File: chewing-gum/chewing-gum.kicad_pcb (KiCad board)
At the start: 2 copper layers, 25.1 x 52.8 mm, 22 parts, among them IC9 INA212AIDCKR, J15 Conn_02x01, J23 Conn_02x01, J28 Conn_01x03, J36 Conn_01x01_Socket, J42 Conn_Coaxial, J62 Conn_01x01_Socket, J78 Conn_01x03, U21 TLV75801PDBV

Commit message: First version of the chewing gum Vdc
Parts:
- removed J62: Conn_01x01_Socket, TestPoint:TestPoint_Keystone_5019_Minature
- removed R93: 48.7k, Resistor_SMD:R_0603_1608Metric
- removed TGND4: TestPoint, TestPoint:TestPoint_THTPad_4.0x4.0mm_Drill2.0mm
- removed TPVBLD3: TestPoint, TestPoint:TestPoint_Plated_Hole_D2.0mm
- added G***: LOGO, heep_footprints:ESL_3x3, B.Cu at (144.8, 59.1)
- added G***: LOGO, heep_footprints:EPFL_2x7, B.Cu at (138.3, 59.1)
- added J10: Conn_01x04, Connector_PinHeader_1.27mm:PinHeader_1x04_P1.27mm_Vertical, F.Cu at (145.9, 102.0)
- added J11: Conn_02x01, Connector_PinHeader_2.54mm:PinHeader_1x02_P2.54mm_Vertical, F.Cu at (136.1, 98.0)
- added J7: Conn_01x06, Connector_PinHeader_1.27mm:PinHeader_1x06_P1.27mm_Vertical, F.Cu at (135.1, 81.0)
- added J8: Conn_01x06, Connector_PinHeader_1.27mm:PinHeader_1x06_P1.27mm_Vertical, F.Cu at (145.8, 81.1)
- added J9: Conn_01x04, Connector_PinHeader_1.27mm:PinHeader_1x04_P1.27mm_Vertical, F.Cu at (135.3, 101.8)
- added R4: 48.7k, Resistor_SMD:R_0603_1608Metric, F.Cu at (138.1, 69.2)
- moved J6 40.8 mm to (137.1, 116.7)
- moved RV1 35.9 mm to (139.9, 85.9), turned to -90 degrees
- moved J3 28.2 mm to (135.3, 78.0), turned to 180 degrees
- moved C2 26.6 mm to (141.2, 90.5)
- moved J4 25.4 mm to (138.6, 90.6), turned to -90 degrees
- moved J2 23.0 mm to (142.8, 96.6)
- moved R1 22.1 mm to (140.5, 67.0)
- moved R5 21.5 mm to (138.8, 77.5)
- moved IC1 21.1 mm to (143.4, 90.8), turned to -90 degrees
- moved R6 20.7 mm to (136.1, 96.7)
- moved D1 19.1 mm to (140.5, 68.6), turned to 0 degrees
- moved R2 18.7 mm to (140.5, 70.2), turned to 180 degrees
- moved R3 18.5 mm to (138.3, 73.0), turned to -90 degrees
- moved C3 18.0 mm to (138.8, 76.0), turned to 180 degrees
- moved J5 17.1 mm to (138.9, 102.6)
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- renumbered C57 to C1, C41 to C2, C58 to C3, IC9 to IC1, J28 to J1, J42 to J2, J78 to J3, J15 to J4, J23 to J5, J36 to J6, R49 to R1, R34 to R2, R41 to R3, R42 to R5, R20 to R6, RV5 to RV1, U21 to U1
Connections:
- net /V_B3_load_n renamed /V_out_test_n
- net /V_B3_o renamed /V_diff_ampl_out
- net /vblade3_ldo renamed /V_ldo_out
- net Net-(J78-Pin_2) renamed /V_ldo_feedback
- C2 pad 1: +3.3VA -> /3V3
- IC1 pad 3: +3.3VA -> /3V3
- IC1 pad 4: /V_B3_INA -> /V_out_test_p
- J1 pad 1: /3V3_LDO -> /3V3
- J1 pad 3: /EN_VBLADE3 -> /LDO_EN_EXT
- J3 pad 3: /DAC4 -> /DAC_ctrl
- J4 pad 2: /V_B3_INA -> /V_out_test_p
- J5 pad 2: /V_B3_load -> /V_out
- J6 pad 1: /V_B3_INA -> /V_out
- R6 pad 2: /V_B3_INA -> /V_out_test_p
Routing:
- net GND: track 29.7 -> 0.00 mm, vias 7 -> 67
- net /EN_VBLADE3: track 26.1 -> 0.00 mm, vias 1 -> 0
- net /V_B3_INA: track 25.8 -> 0.00 mm
- net /V_B3_load: track 17.7 -> 0.00 mm, vias 1 -> 0
- net /DAC_ctrl: track 0.00 -> 15.8 mm
- net /V_out_test_p: track 0.00 -> 12.4 mm
- net /LDO_EN_EXT: track 0.00 -> 9.71 mm
- net /V_out: track 0.00 -> 8.92 mm
- net /V_diff_ampl_out: track 8.79 -> 16.0 mm
- net Net-(D1-A): track 15.7 -> 9.81 mm
- net /V_out_test_n: track 14.3 -> 18.0 mm
- net /V_ldo_out: track 17.5 -> 21.1 mm, vias 3 -> 0
- net /DAC4: track 2.98 -> 0.00 mm
- net +3.3VA: track 2.15 -> 0.00 mm, vias 1 -> 0
- net Net-(R5-Pad1): track 5.16 -> 3.42 mm
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- added copper zone on B.Cu, net (none)
- added copper zone on F.Cu, net /3V3
- added copper zone on F.Cu, net /V_ldo_feedback
- added copper zone on B.Cu, net GND
- added copper zone on F.Cu, net GND
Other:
- board size 25.1 x 52.8 mm -> 13.1 x 49.3 mm
- board text added: "(LDO)"
- board text added: "(ampl)"
- board text added: "(shunt)"
- board text added: "(trimmer)"
- board text added: "+-"
- board text added: "Chewing-gum: V - v1.0 - 09/25"
- board text added: "DAC ctrl▶"
- board text added: "DC"
- board text added: "Ext. En"
- board text added: "GND"
- board text added: "LDO fb▶"
- board text added: "LDOout◀"
- board text added: "NC"
- board text added: "R6←LDO"
- board text added: "R6→out"
- board text added: "Vout"
- board text added: "▶"
- board text added: "▶Vdiff"
- board text added: "◀3V3"
- board text added: "◀Ext. EN"
- board text added: "◀Ref.Ampl."
- board text removed: "I2C enable"
- board text removed: "VBLADE2"

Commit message: Finished ADC/DAC board
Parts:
- removed J6: Conn_01x01_Socket, Connector:Banana_Jack_1Pin
- moved J9 0.38 mm to (135.1, 102.1)
- moved J8 0.10 mm to (145.9, 81.0)
- moved J7 0.07 mm to (135.1, 81.0)
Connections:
- J10 pad 3: /V_diff_ampl_out -> unconnected-(J10-Pin_3-Pad3)
- J10 pad 4: unconnected-(J10-Pin_4-Pad4) -> /V_diff_ampl_out
- J8 pad 3: GND -> unconnected-(J8-Pin_3-Pad3)
- J8 pad 4: unconnected-(J8-Pin_4-Pad4) -> GND
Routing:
- net /V_out: track 8.92 -> 0.62 mm
- net /V_diff_ampl_out: track 16.0 -> 16.8 mm
- net GND: vias 67 -> 71
- added copper zone on F.Cu, net /V_out

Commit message: Before re-organizing the main board
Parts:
- moved C1 1.66 mm to (141.8, 75.3), turned to 180 degrees
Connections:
- C1 pad 1: /Vpm -> /5V
- J8 pad 2: unconnected-(J8-Pin_2-Pad2) -> /5V
- J8 pad 3: unconnected-(J8-Pin_3-Pad3) -> /5V
- U1 pad 1: /Vpm -> /5V
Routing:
- net /Vpm: track 2.43 -> 0.00 mm
- net GND: vias 71 -> 68
- added copper zone on F.Cu, net /5V
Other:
- board text added: "◀5V"

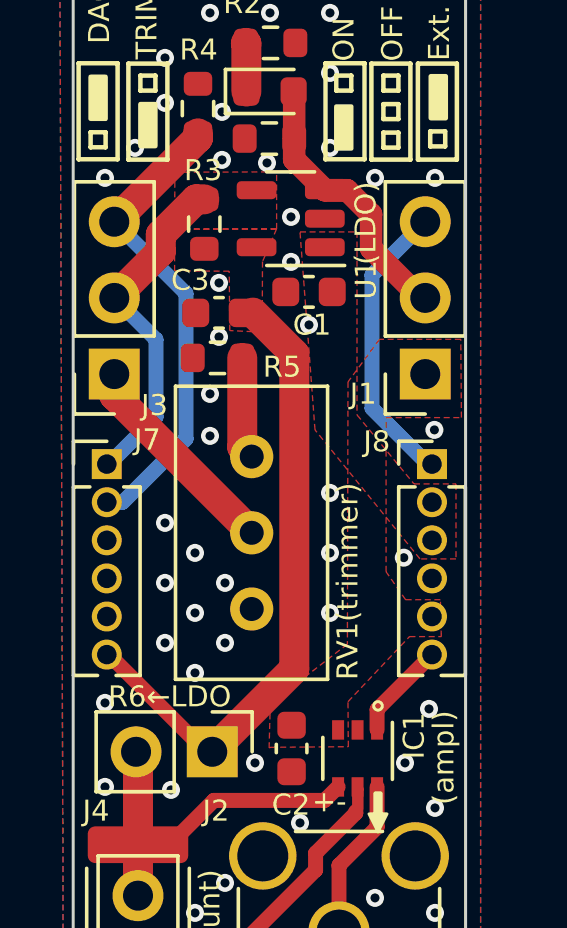
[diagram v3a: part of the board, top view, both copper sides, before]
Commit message: Before re-routing programmer
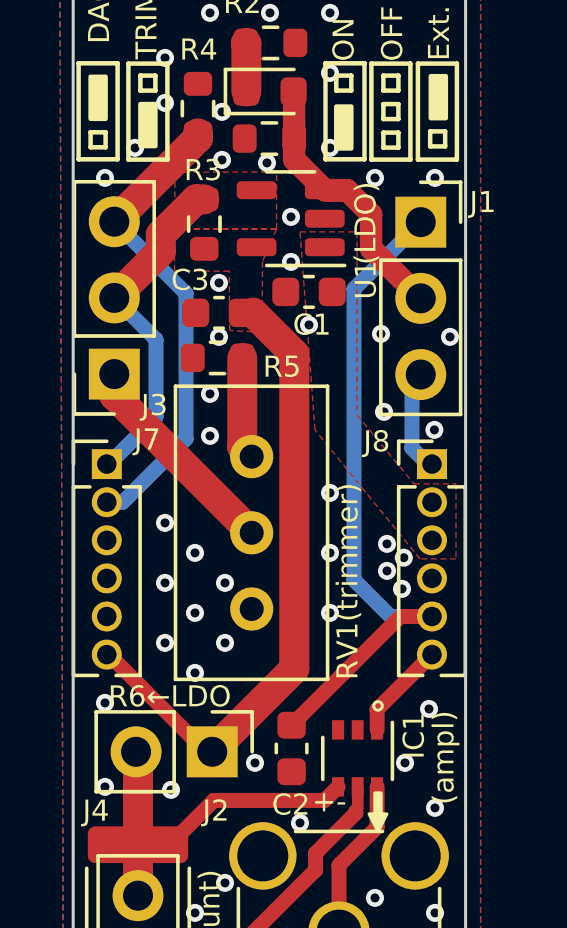
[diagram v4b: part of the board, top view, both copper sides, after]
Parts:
- moved J1 5.07 mm to (145.5, 73.0), turned to 0 degrees
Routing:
- net /3V3: track 0.00 -> 22.1 mm
- net /LDO_EN_EXT: track 9.71 -> 3.45 mm
- net GND: vias 68 -> 74
- removed copper zone on F.Cu, net /3V3
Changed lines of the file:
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@@
 	(footprint "Connector_PinSocket_2.54mm:PinSocket_1x03_P2.54mm_Vertical"
 		(layer "F.Cu")
-		(at 145.675 78.04 180)
+		(at 145.525 72.975)
 		(descr "Through hole straight socket strip, 1x03, 2.54mm pitch, single row (from Kicad 4.0.7), script generated")
 		(tags "Through hole socket strip THT 1x03 2.54mm single row")
 		(property "Reference" "J1"
-			(at 2.07 -0.66 0)
+			(at 2.07 -0.66 360)
 			(layer "F.SilkS")
 			(effects
@@
 		)
 		(property "Value" "Conn_01x03"
-			(at 0 7.85 0)
+			(at 0 7.85 360)
 			(layer "F.Fab")
 			(effects
@@
 		)
 		(property "Footprint" "Connector_PinSocket_2.54mm:PinSocket_1x03_P2.54mm_Vertical"
-			(at 0 0 0)
+			(at 0 0 360)
 			(layer "F.Fab")
 			(hide yes)
@@
 		)
 		(property "Datasheet" ""
-			(at 0 0 0)
+			(at 0 0 360)
 			(layer "F.Fab")
 			(hide yes)
@@
 		)
 		(property "Description" ""
-			(at 0 0 0)
+			(at 0 0 360)
 			(layer "F.Fab")
 			(hide yes)
@@
 		(attr through_hole exclude_from_pos_files)
 		(fp_line
-			(start 1.33 1.27)
-			(end 1.33 6.41)
+			(start -1.33 1.27)
+			(end -1.33 6.41)
 			(stroke
 				(width 0.12)
@@
 		)
 		(fp_line
-			(start 1.33 -1.33)
-			(end 1.33 0)
+			(start -1.33 1.27)
+			(end 1.33 1.27)
 			(stroke
 				(width 0.12)
@@
 		)
 		(fp_line
-			(start 0 -1.33)
-			(end 1.33 -1.33)
+			(start -1.33 6.41)
+			(end 1.33 6.41)
 			(stroke
 				(width 0.12)
@@
 		)
 		(fp_line
-			(start -1.33 6.41)
-			(end 1.33 6.41)
+			(start 0 -1.33)
+			(end 1.33 -1.33)
 			(stroke
 				(width 0.12)
@@
 		)
 		(fp_line
-			(start -1.33 1.27)
-			(end 1.33 1.27)
+			(start 1.33 -1.33)
+			(end 1.33 0)
 			(stroke
 				(width 0.12)
@@
 		)
 		(fp_line
-			(start -1.33 1.27)
-			(end -1.33 6.41)
+			(start 1.33 1.27)
+			(end 1.33 6.41)
 			(stroke
 				(width 0.12)
@@
 		)
 		(fp_line
-			(start 1.75 6.85)
-			(end -1.8 6.85)
+			(start -1.8 -1.8)
+			(end 1.75 -1.8)
 			(stroke
 				(width 0.05)
@@
 		)
 		(fp_line
-			(start 1.75 -1.8)
-			(end 1.75 6.85)
+			(start -1.8 6.85)
+			(end -1.8 -1.8)
 			(stroke
 				(width 0.05)
@@
 		)
 		(fp_line
-			(start -1.8 6.85)
-			(end -1.8 -1.8)
+			(start 1.75 -1.8)
+			(end 1.75 6.85)
 			(stroke
 				(width 0.05)
@@
 		)
 		(fp_line
-			(start -1.8 -1.8)
-			(end 1.75 -1.8)
+			(start 1.75 6.85)
+			(end -1.8 6.85)
 			(stroke
 				(width 0.05)
@@
 		)
 		(fp_line
-			(start 1.27 6.35)
-			(end -1.27 6.35)
+			(start -1.27 -1.27)
+			(end 0.635 -1.27)
 			(stroke
 				(width 0.1)
@@
 		)
 		(fp_line
-			(start 1.27 -0.635)
-			(end 1.27 6.35)
+			(start -1.27 6.35)
+			(end -1.27 -1.27)
 			(stroke
 				(width 0.1)
@@
 		)
 		(fp_line
-			(start -1.27 6.35)
-			(end -1.27 -1.27)
+			(start 1.27 -0.635)
+			(end 1.27 6.35)
 			(stroke
 				(width 0.1)
@@
 		)
 		(fp_line
-			(start -1.27 -1.27)
-			(end 0.635 -1.27)
+			(start 1.27 6.35)
+			(end -1.27 6.35)
 			(stroke
 				(width 0.1)
@@
 		)
 		(pad "1" thru_hole rect
-			(at 0 0 180)
+			(at 0 0)
 			(size 1.7 1.7)
 			(drill 1)
@@
 		)
 		(pad "2" thru_hole oval
-			(at 0 2.54 180)
+			(at 0 2.54)
 			(size 1.7 1.7)
 			(drill 1)
@@
 		)
 		(pad "3" thru_hole oval
-			(at 0 5.08 180)
+			(at 0 5.08)
 			(size 1.7 1.7)
 			(drill 1)
@@
 		)
 		(property "Value" "10u"
-			(at 0 1.43 360)
+			(at 0 1.43 0)
 			(layer "F.Fab")
 			(effects
@@
 		)
 		(property "Footprint" "Capacitor_SMD:C_0603_1608Metric"
-			(at 0 0 360)
+			(at 0 0 0)
 			(layer "F.Fab")
 			(hide yes)
@@
 		)
 		(property "Datasheet" ""
-			(at 0 0 360)
+			(at 0 0 0)
 			(layer "F.Fab")
 			(hide yes)
@@
 		)
 		(property "Description" ""
-			(at 0 0 360)
+			(at 0 0 0)
 			(layer "F.Fab")
 			(hide yes)
@@
 		)
 		(fp_text user "${REFERENCE}"
-			(at 0 0 360)
+			(at 0 0 0)
 			(layer "F.Fab")
 			(effects
@@
 	)
 	(via
+		(at 144.4 84.6)
+		(size 0.6)
+		(drill 0.3)
+		(layers "F.Cu" "B.Cu")
+		(free yes)
+		(net 1)
+	)
+	(via
 		(at 144.5 106)
 		(size 0.6)
@@
 	)
 	(via
+		(at 144.2 76.7)
+		(size 0.6)
+		(drill 0.3)
+		(layers "F.Cu" "B.Cu")
+		(free yes)
+		(net 1)
+	)
+	(via
 		(at 139 95)
 		(size 0.6)
@@
 	)
 	(via
+		(at 144.3 79.3)
+		(size 0.6)
+		(drill 0.3)
+		(layers "F.Cu" "B.Cu")
+		(free yes)
+		(net 1)
+	)
+	(via
 		(at 135 71.5)
 		(size 0.6)
@@
 	)
 	(via
+		(at 146.5 76.8)
+		(size 0.6)
+		(drill 0.3)
+		(layers "F.Cu" "B.Cu")
+		(free yes)
+		(net 1)
+	)
+	(via
 		(at 138.8 75)
 		(size 0.6)
@@
 	)
 	(via
+		(at 144.4 83.7)
+		(size 0.6)
+		(drill 0.3)
+		(layers "F.Cu" "B.Cu")
+		(free yes)
+		(net 1)
+	)
+	(via
 		(at 138.8 76.8)
 		(size 0.6)
@@
 		(net 1)
 	)
+	(via
+		(at 144.9 85.2)
+		(size 0.6)
+		(drill 0.3)
+		(layers "F.Cu" "B.Cu")
+		(free yes)
+		(net 1)
+	)
 	(segment
 		(start 139.7125 67.0175)
@@
 	)
 	(segment
-		(start 143.9 74.735)
-		(end 145.675 72.96)
+		(start 144.845 86.12)
+		(end 145.9 86.12)
+		(width 0.5)
+		(layer "F.Cu")
+		(net 6)
+	)
+	(segment
+		(start 141.22 89.745)
+		(end 144.845 86.12)
+		(width 0.5)
+		(layer "F.Cu")
+		(net 6)
+	)
+	(segment
+		(start 144.52 86.12)
+		(end 143.3 84.9)
+		(width 0.5)
+		(layer "B.Cu")
+		(net 6)
+	)
+	(segment
+		(start 143.3 84.9)
+		(end 143.3 75.2)
+		(width 0.5)
+		(layer "B.Cu")
+		(net 6)
+	)
+	(segment
+		(start 145.9 86.12)
+		(end 144.52 86.12)
+		(width 0.5)
+		(layer "B.Cu")
+		(net 6)
+	)
+	(segment
+		(start 143.3 75.2)
+		(end 145.525 72.975)
+		(width 0.5)
+		(layer "B.Cu")
+		(net 6)
+	)
+	(segment
+		(start 145.23 78.35)
+		(end 145.525 78.055)
 		(width 0.5)
 		(layer "B.Cu")
@@
 	(segment
 		(start 145.85 81.13)
-		(end 143.9 79.18)
+		(end 145.23 80.51)
 		(width 0.5)
 		(layer "B.Cu")
@@
 	)
 	(segment
-		(start 143.9 79.18)
-		(end 143.9 74.735)
+		(start 145.23 80.51)
+		(end 145.23 78.35)
 		(width 0.5)
 		(layer "B.Cu")
@@
 			)
 		)
-	)
-	(zone
-		(net 6)
-		(net_name "/3V3")
-		(layer "F.Cu")
-		(hatch edge 0.5)
-		(priority 2)
-		(connect_pads yes
-			(clearance 0.1)
-		)
-		(min_thickness 0.25)
-		(filled_areas_thickness no)
-		(fill yes
-			(thermal_gap 0.5)
-			(thermal_bridge_width 0.5)
-		)
-		(polygon
-			(pts
-				(xy 140.52 90.48) (xy 143.11 90.46) (xy 143.1 88.96) (xy 145.15 86.79) (xy 146.21 86.79) (xy 146.18 85.56)
-				(xy 145.02 85.56) (xy 144.37 84.63) (xy 144.37 79.49) (xy 146.88 79.49) (xy 146.86 76.88) (xy 144.15 76.88)
-				(xy 143.1 78.3) (xy 143.08 87.04) (xy 140.51 89.03) (xy 140.47 90.5)
-			)
-		)
